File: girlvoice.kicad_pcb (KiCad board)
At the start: 4 copper layers, 43.1 x 42.5 mm, 150 parts, among them J1 IPS 1.28 inch SPI GC9A01, J2 Pico, J3 PAJ7620F2, J7 USB_C, J8 AudioJack4_SwitchTR1, Q1 BSS214NW, Q2 AO3401A, SW1 ON/OFF, SW2 UP, SW3 DOWN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

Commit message: ADD: Fabrication instructions
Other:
- board text added: "When panalizing the PCB, make sure the mousebits are not under the connector since it has overhang."
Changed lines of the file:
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@@
 		)
 		(fp_text user "${REFERENCE}"
-			(at 0 1.9 180)
+			(at 0 1.6 180)
 			(layer "F.Fab")
 			(effects
@@
 		)
 		(property "Value" "PMEG40T20ER"
-			(at 0 2 90)
+			(at 0 1.4 90)
 			(layer "F.Fab")
 			(effects
 				(font
-					(size 1 1)
-					(thickness 0.15)
+					(size 0.3 0.3)
+					(thickness 0.075)
 				)
 			)
@@
 		)
 		(fp_text user "${REFERENCE}"
-			(at 0 -2 90)
+			(at 0.375 -1.6 90)
 			(layer "F.Fab")
 			(effects
@@
 			(at 0 1.68 0)
 			(layer "F.Fab")
+			(hide yes)
 			(effects
 				(font
@@
 			(at 0 1.68 180)
 			(layer "F.Fab")
+			(hide yes)
 			(effects
 				(font
@@
 			(at 0 1.68 90)
 			(layer "F.Fab")
+			(hide yes)
 			(effects
 				(font
@@
 		(layer "B.Fab")
 	)
+	(gr_line
+		(start 117.5 117.25)
+		(end 118.75 116)
+		(stroke
+			(width 0.1)
+			(type default)
+		)
+		(layer "F.Fab")
+	)
+	(gr_line
+		(start 121 117.25)
+		(end 117.5 117.25)
+		(stroke
+			(width 0.1)
+			(type default)
+		)
+		(layer "F.Fab")
+	)
+	(gr_line
+		(start 118.75 118.5)
+		(end 117.5 117.25)
+		(stroke
+			(width 0.1)
+			(type default)
+		)
+		(layer "F.Fab")
+	)
 	(gr_text "CDONE\n"
 		(at 100.1 117.6 90)
@@
 			)
 			(justify left bottom)
+		)
+	)
+	(gr_text "When panalizing the PCB, \nmake sure the mousebits are not \nunder the connector \nsince it has overhang.\n"
+		(at 121.5 119.5 0)
+		(layer "F.Fab")
+		(effects
+			(font
+				(size 1 1)
+				(thickness 0.1)
+			)
+			(justify left bottom)

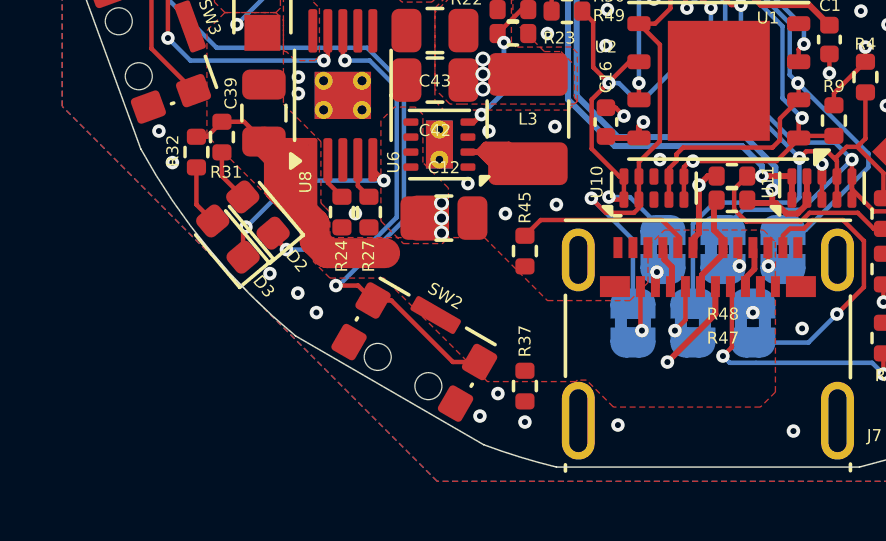
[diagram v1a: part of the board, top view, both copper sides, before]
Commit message: UPD: connect pushbutton shield to groundplane for better mechanical support
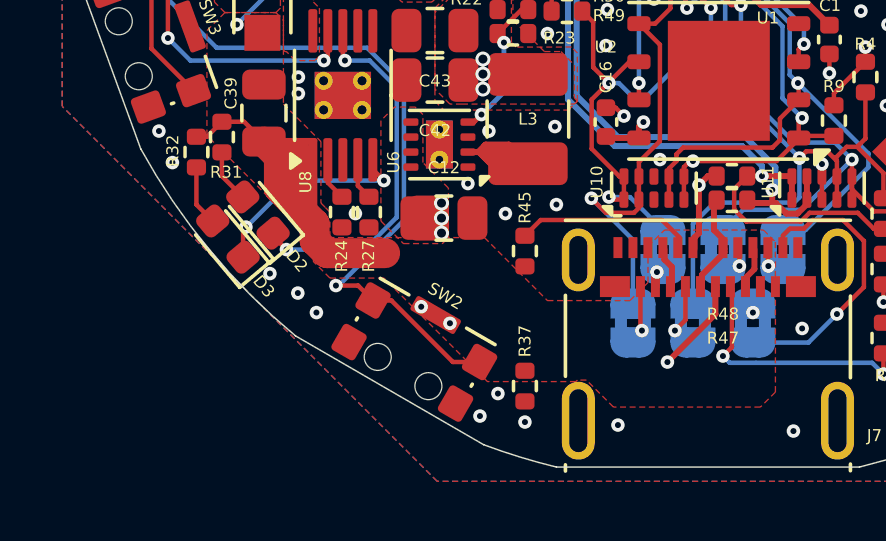
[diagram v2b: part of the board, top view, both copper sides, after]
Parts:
- J8: value AudioJack4_SwitchTR1 -> AudioJack 2.5mm
- U1: value LIFCL40-NX -> LIFCL-17-8SG72C
- U9: value MAX98357A -> MAX98357A - DNP
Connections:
- SW1 pad SH: (no net) -> GND
- SW2 pad SH: (no net) -> GND
- SW3 pad SH: (no net) -> GND
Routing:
- net GND: vias 180 -> 182
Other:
- board text added: "GirlVoice rev1.1 CrosslinkNX Vocoder DSP: Sage CAD: Fait PCB: Lucy 2024"
- board text removed: "GirlVoice rev1.0 CrosslinkNX Vocoder DSP: Sage CAD: Fait PCB: Lucy 2024"
